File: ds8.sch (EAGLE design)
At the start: 92 parts, among them IC1 TM4C1230C3PM, IC2 TPS77333, J1 9VDC, Q1 BC850, Q2 BC850, Q3 BC850, U1 LM13700M, U2 LM324, U3 LM324, U4 LM741D, X1 MAB5SH

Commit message: added more decoupling to vdd pins. jtag in place with a reset line
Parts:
- added C16, C17, C18, C19, C20, C21: 0.01uF, rcl:C-EUC1206
- added JP3: (no value), SparkFun-Connectors:M05PTH
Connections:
- removed net /RESET: IC1.RST, IC2.!RESET, R40.1
- new net N$41: IC1.RST, JP3.5, R40.1
- new net N$42: C21.2, IC1.VDDC@0
- new net TCK: IC1.TCK, JP3.1
- new net TDI: IC1.TDI, JP3.4
- new net TDO: IC1.TDO, JP3.3
- new net TMS: IC1.TMS, JP3.2
- net ARM_SSI0_FS: no longer U$1.SCLK
- net GND: now also C16.1, C17.2, C18.1, C19.1, C20.1, C21.1
- net N$6: now also U$1.SCLK; no longer C14.2, IC1.VDDC@0
- net SWCLK: no longer IC1.TCK
- net SWDIO: no longer IC1.TMS
- net VDD: now also C14.2, C16.2, C17.1, C18.2, C19.2, C20.2
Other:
- moved on the sheet: C14, R40

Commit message: TODO : Check JTAG
Don't we need to have at least a common ground for the JTAG connection ? What about using this kind of supposedly standard header ? http://www.keil.com/support/man/docs/ulinkpro/ulinkpro_hw_if_jtag10.htm
Done : board rerouted, added test points, added screw holes, moved a few things around, almost ready to be produced once we are sure about the JTAG stuff & checked the components one last time.

Signed-off-by: Kamel Makhloufi <melka@blaste.net>
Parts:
- removed JP1: (no value), SparkFun-Connectors:AUDIO-JACK2.5MM
- added IC3: DAC7512, ds8:DAC7512
- added TP1, TP10, TP11, TP12, TP13, TP14, TP2, TP3, TP4, TP5, TP6, TP7, TP8, TP9: TEST-POINT3X5, SparkFun-Passives:TEST-POINT3X5
- C15: value 3uF -> 0.01uF
- C18: value 0.01uF -> 3uF
- J1: value 9VDC -> 9VDC POSITIVE CENTER
- JP3: value (none) -> JTAG
- RV1: value TRIMPOT -> TRIGGER SENSITIVITY
- U$1: value DAC7512 -> 6.35MMJACK; device ds8:DAC7512 -> ds8:6.35MMJACK
- U1: device ds8:LM13700M -> ds8:DS8_LM13700M
- X1: value MAB5SH -> MIDI IN
- gave numbers to parts that had none: 1
- renumbered C?1 to C23, U$2 to U100
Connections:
- net N$41 renamed RST
- removed net N$6: U$1.SCLK
- removed net SWCLK: X1.1
- removed net SWDIO: X1.3
- net 9VDC: now also TP2.1
- net ARM_SSI0_CLK: now also IC3.SCLK, TP10.1
- net ARM_SSI0_FS: now also IC3./SYNC, TP11.1; no longer U$1./SYNC
- net ARM_SSI0_TX: now also IC3.DIN, TP9.1; no longer U$1.DIN
- net CVIN: now also IC3.VOUT, TP7.1; no longer U$1.VOUT
- net GND: now also C15.1, C18.2, IC3.GND, TP12.1, TP14.1, TP5.1, TP6.1, TP8.1, U$1.S, X1.PE; no longer C15.2, C18.1, JP1.SLEEVE, U$1.GND
- net MIDI_IN: now also TP1.1
- net MIDI_TRIG: now also TP13.1
- net N$36: now also C18.1; no longer C15.1
- net N$42: now also C16.2; no longer C21.2
- net N$57: now also U$1.R, U$1.T; no longer JP1.LEFT, JP1.RIGHT
- net VCC: now also IC3.VDD, TP3.1; no longer U$1.VDD
- net VDD: now also C15.2, C21.2, TP4.1; no longer C16.2, C18.2
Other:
- moved on the sheet: C15, C16, C17, C18, C21, R40

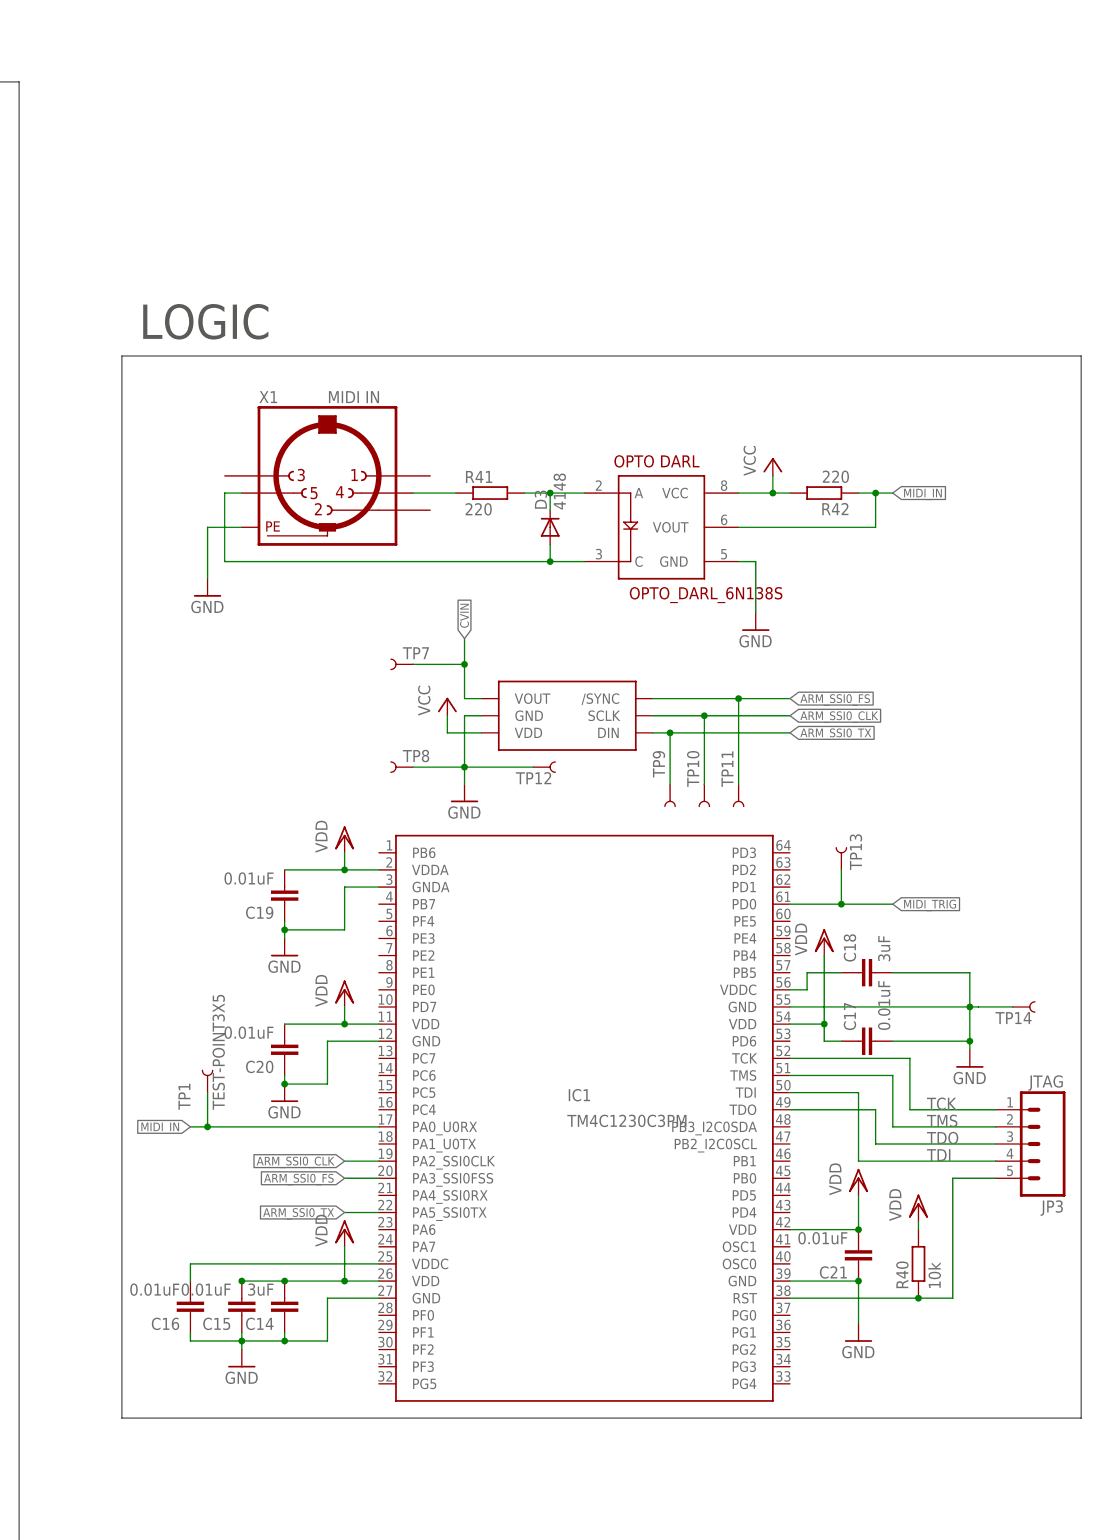
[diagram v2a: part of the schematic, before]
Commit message: PCB v1 Release
Added GND on JTAG and a MIDI Passthrough connector

Signed-off-by: Kamel Makhloufi <melka@blaste.net>
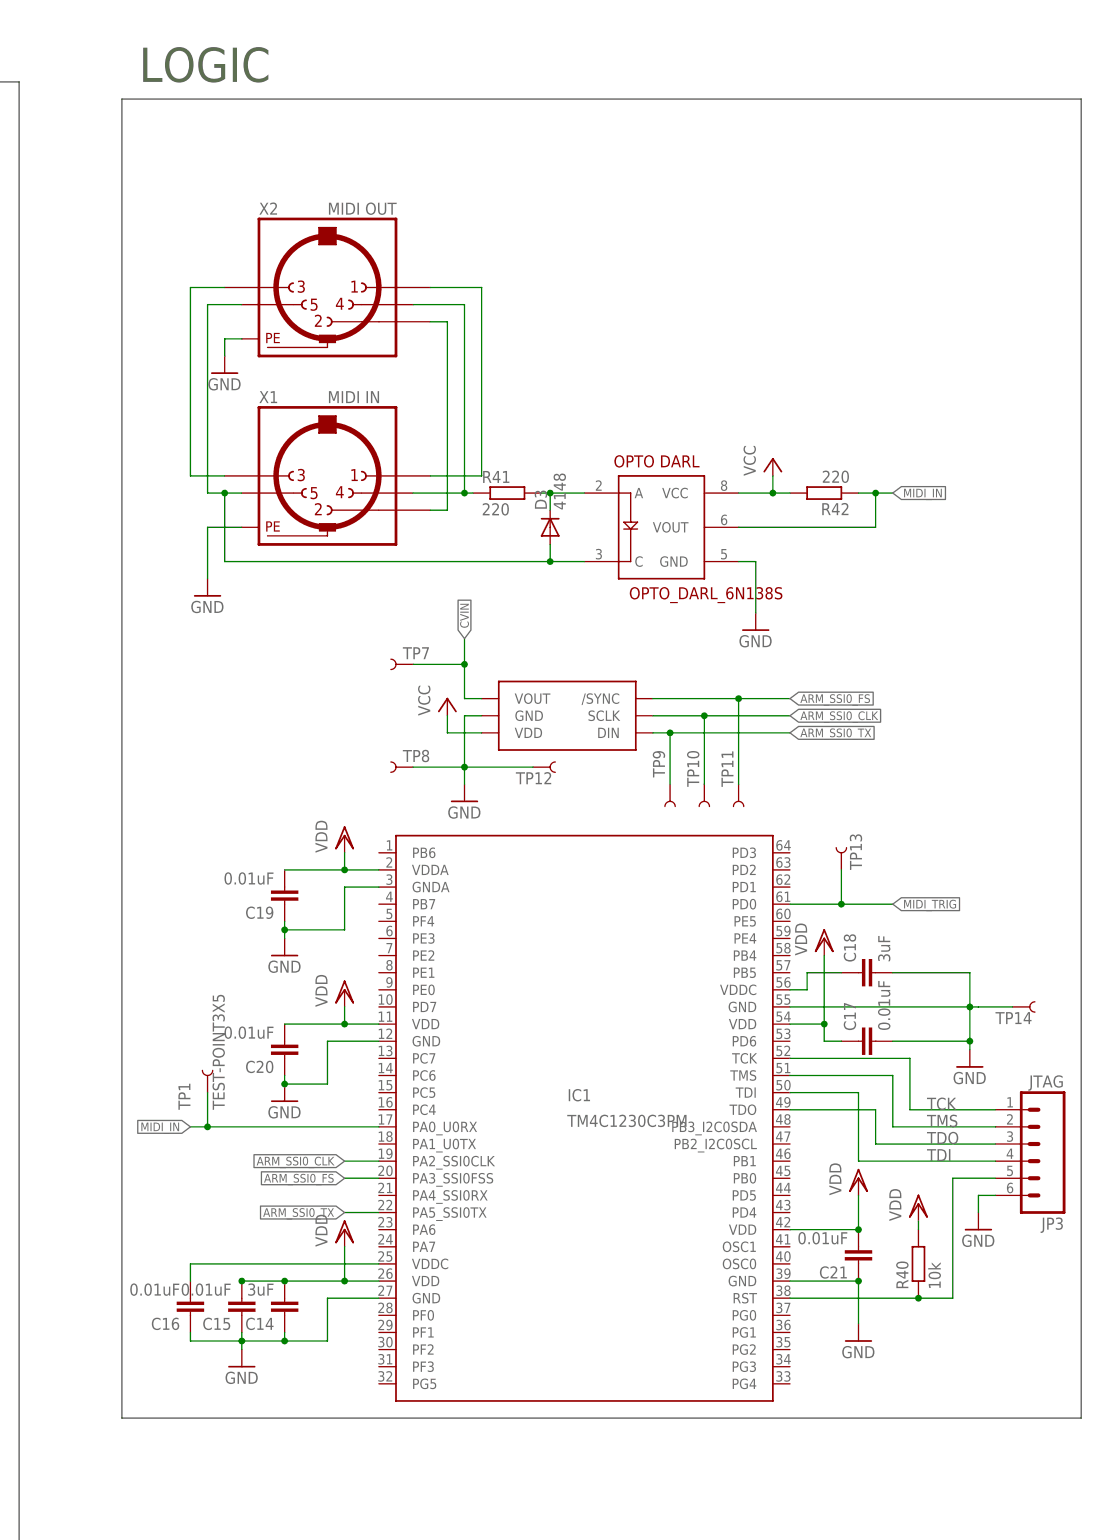
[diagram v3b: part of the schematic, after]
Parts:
- added X2: MIDI OUT, con-hirschmann:MAB5SH
- JP3: device SparkFun-Connectors:M05PTH -> SparkFun-Connectors:M06SIP
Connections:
- new net N$41: X1.2, X2.2
- new net N$43: X1.3, X2.3
- new net N$6: X1.1, X2.1
- net GND: now also JP3.6, X2.PE
- net N$18: now also X2.4
- net N$35: now also X2.5
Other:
- moved on the sheet: R41
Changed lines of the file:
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@@
 <part name="U$3" library="ds8" deviceset="ALPS_SRBV" device=""/>
 <part name="U$4" library="SparkFun-DiscreteSemi" deviceset="OPTO_DARL_6N138S" device=""/>
-<part name="JP3" library="SparkFun-Connectors" deviceset="M05" device="PTH" value="JTAG"/>
+<part name="JP3" library="SparkFun-Connectors" deviceset="M06" device="SIP" value="JTAG"/>
 <part name="VDD7" library="supply1" deviceset="VDD" device=""/>
 <part name="R40" library="rcl" deviceset="R-EU_" device="M0805" value="10k"/>
@@
 <part name="TP13" library="SparkFun-Passives" deviceset="TEST-POINT" device="3X5"/>
 <part name="TP14" library="SparkFun-Passives" deviceset="TEST-POINT" device="3X5"/>
+<part name="X2" library="con-hirschmann" deviceset="MAB5SH" device="" value="MIDI OUT">
+<attribute name="MF" value=""/>
+<attribute name="MPN" value=""/>
+<attribute name="OC_FARNELL" value="809883"/>
+<attribute name="OC_NEWARK" value="unknown"/>
+</part>
+<part name="GND24" library="supply1" deviceset="GND" device=""/>
+<part name="GND26" library="supply1" deviceset="GND" device=""/>
 </parts>
 <sheets>
@@
 <wire x1="-127" y1="55.88" x2="-127" y2="-10.16" width="0.1524" layer="97"/>
 <text x="-124.46" y="-7.62" size="5.08" layer="97">5V -&gt; 3.3V</text>
-<text x="314.96" y="22.86" size="5.08" layer="97">LOGIC</text>
+<text x="314.96" y="60.96" size="5.08" layer="97">LOGIC</text>
 <wire x1="312.42" y1="-137.16" x2="454.66" y2="-137.16" width="0.1524" layer="97"/>
-<wire x1="454.66" y1="-137.16" x2="454.66" y2="20.32" width="0.1524" layer="97"/>
-<wire x1="454.66" y1="20.32" x2="312.42" y2="20.32" width="0.1524" layer="97"/>
-<wire x1="312.42" y1="20.32" x2="312.42" y2="-137.16" width="0.1524" layer="97"/>
+<wire x1="454.66" y1="-137.16" x2="454.66" y2="58.42" width="0.1524" layer="97"/>
+<wire x1="454.66" y1="58.42" x2="312.42" y2="58.42" width="0.1524" layer="97"/>
+<wire x1="312.42" y1="58.42" x2="312.42" y2="-137.16" width="0.1524" layer="97"/>
 <wire x1="33.02" y1="-76.2" x2="76.2" y2="-76.2" width="0.1524" layer="97"/>
 <wire x1="76.2" y1="-76.2" x2="76.2" y2="-127" width="0.1524" layer="97"/>
@@
 <instance part="X1" gate="G$1" x="342.9" y="2.54"/>
 <instance part="P+12" gate="VCC" x="408.94" y="5.08"/>
-<instance part="R41" gate="G$1" x="367.03" y="0"/>
+<instance part="R41" gate="G$1" x="369.57" y="0"/>
 <instance part="R42" gate="G$1" x="416.56" y="0" rot="R180"/>
 <instance part="GND41" gate="1" x="406.4" y="-20.32"/>
@@
 <instance part="U$3" gate="G$1" x="-165.1" y="-97.79"/>
 <instance part="U$4" gate="G$1" x="391.16" y="-2.54"/>
-<instance part="JP3" gate="G$1" x="449.58" y="-96.52" rot="R180"/>
+<instance part="JP3" gate="G$1" x="447.04" y="-96.52" rot="R180"/>
 <instance part="VDD7" gate="G$1" x="430.53" y="-105.41"/>
 <instance part="R40" gate="G$1" x="430.53" y="-114.3" rot="R90"/>
@@
 <attribute name="NAME" x="441.96" y="-78.74" size="1.778" layer="95"/>
 </instance>
+<instance part="X2" gate="G$1" x="342.9" y="30.48"/>
+<instance part="GND24" gate="1" x="327.66" y="17.78"/>
+<instance part="GND26" gate="1" x="439.42" y="-109.22"/>
 </instances>
 <busses>
@@
 <wire x1="325.12" y1="-5.08" x2="325.12" y2="-12.7" width="0.1524" layer="91"/>
 </segment>
+<segment>
+<pinref part="X2" gate="G$1" pin="PE"/>
+<wire x1="330.2" y1="22.86" x2="327.66" y2="22.86" width="0.1524" layer="91"/>
+<wire x1="327.66" y1="22.86" x2="327.66" y2="20.32" width="0.1524" layer="91"/>
+<pinref part="GND24" gate="1" pin="GND"/>
+</segment>
+<segment>
+<pinref part="JP3" gate="G$1" pin="6"/>
+<pinref part="GND26" gate="1" pin="GND"/>
+<wire x1="441.96" y1="-104.14" x2="439.42" y2="-104.14" width="0.1524" layer="91"/>
+<wire x1="439.42" y1="-104.14" x2="439.42" y2="-106.68" width="0.1524" layer="91"/>
+</segment>
 </net>
 <net name="VCC" class="0">
@@
 <pinref part="X1" gate="G$1" pin="4"/>
 <pinref part="R41" gate="G$1" pin="1"/>
-<wire x1="355.6" y1="0" x2="361.95" y2="0" width="0.1524" layer="91"/>
+<wire x1="355.6" y1="0" x2="363.22" y2="0" width="0.1524" layer="91"/>
+<pinref part="X2" gate="G$1" pin="4"/>
+<wire x1="363.22" y1="0" x2="364.49" y2="0" width="0.1524" layer="91"/>
+<wire x1="355.6" y1="27.94" x2="363.22" y2="27.94" width="0.1524" layer="91"/>
+<wire x1="363.22" y1="27.94" x2="363.22" y2="0" width="0.1524" layer="91"/>
+<junction x="363.22" y="0"/>
 </segment>
 </net>
@@
 <segment>
 <pinref part="R41" gate="G$1" pin="2"/>
-<wire x1="372.11" y1="0" x2="375.92" y2="0" width="0.1524" layer="91"/>
+<wire x1="374.65" y1="0" x2="375.92" y2="0" width="0.1524" layer="91"/>
 <wire x1="375.92" y1="0" x2="381" y2="0" width="0.1524" layer="91"/>
 <wire x1="375.92" y1="-2.54" x2="375.92" y2="0" width="0.1524" layer="91"/>
@@
 <junction x="375.92" y="-10.16"/>
 <pinref part="U$4" gate="G$1" pin="C"/>
+<wire x1="327.66" y1="0" x2="325.12" y2="0" width="0.1524" layer="91"/>
+<wire x1="325.12" y1="0" x2="325.12" y2="27.94" width="0.1524" layer="91"/>
+<pinref part="X2" gate="G$1" pin="5"/>
+<wire x1="325.12" y1="27.94" x2="330.2" y2="27.94" width="0.1524" layer="91"/>
+<junction x="327.66" y="0"/>
 </segment>
 </net>
@@
 </segment>
 </net>
+<net name="N$6" class="0">
+<segment>
+<pinref part="X1" gate="G$1" pin="1"/>
+<wire x1="358.14" y1="2.54" x2="365.76" y2="2.54" width="0.1524" layer="91"/>
+<wire x1="365.76" y1="2.54" x2="365.76" y2="30.48" width="0.1524" layer="91"/>
+<pinref part="X2" gate="G$1" pin="1"/>
+<wire x1="365.76" y1="30.48" x2="358.14" y2="30.48" width="0.1524" layer="91"/>
+</segment>
+</net>
+<net name="N$41" class="0">
+<segment>
+<pinref part="X2" gate="G$1" pin="2"/>
+<wire x1="358.14" y1="25.4" x2="360.68" y2="25.4" width="0.1524" layer="91"/>
+<wire x1="360.68" y1="25.4" x2="360.68" y2="-2.54" width="0.1524" layer="91"/>
+<pinref part="X1" gate="G$1" pin="2"/>
+<wire x1="360.68" y1="-2.54" x2="358.14" y2="-2.54" width="0.1524" layer="91"/>
+</segment>
+</net>
+<net name="N$43" class="0">
+<segment>
+<pinref part="X2" gate="G$1" pin="3"/>
+<wire x1="327.66" y1="30.48" x2="322.58" y2="30.48" width="0.1524" layer="91"/>
+<wire x1="322.58" y1="30.48" x2="322.58" y2="2.54" width="0.1524" layer="91"/>
+<pinref part="X1" gate="G$1" pin="3"/>
+<wire x1="322.58" y1="2.54" x2="327.66" y2="2.54" width="0.1524" layer="91"/>
+</segment>
+</net>
